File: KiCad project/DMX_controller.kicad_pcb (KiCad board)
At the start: 2 copper layers, 8 parts, among them J1 DMX_output, SW1 SW_Push_DPDT, U1 TTL_to_RS485_transceiver

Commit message: Make a real PCB!
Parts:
- added REF**: MountingHole_3.2mm_M3, MountingHole:MountingHole_3.2mm_M3, F.Cu at (53.3, 43.2)
- added REF**: MountingHole_3.2mm_M3, MountingHole:MountingHole_3.2mm_M3, F.Cu at (172.7, 149.9)
- added REF**: MountingHole_3.2mm_M3, MountingHole:MountingHole_3.2mm_M3, F.Cu at (53.3, 149.9)
- added REF**: MountingHole_3.2mm_M3, MountingHole:MountingHole_3.2mm_M3, F.Cu at (172.7, 43.2)
- RV3: value slider_3_hue -> slider_3_saturation
- RV4: value slider_4_saturation -> slider_4_hue
- moved U1 31.4 mm to (149.9, 98.9), turned to -90 degrees
- moved J1 20.5 mm to (155.1, 53.3)
- moved SW1 14.4 mm to (154.6, 103.1), turned to 90 degrees
- moved A1 9.16 mm to (149.9, 91.4)
- moved RV3 2.54 mm to (96.2, 52.3)
- moved RV4 2.54 mm to (114.5, 52.3)
- moved RV2 2.54 mm to (78.7, 52.3)
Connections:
- net /5V renamed +5V
- A1 pad 29: /GND -> unconnected-(A1-Pad29)
- A1 pad 4: /GND -> GND
- RV1 pad 1: /GND -> GND
- RV2 pad 1: /GND -> GND
- RV3 pad 1: /GND -> GND
- RV4 pad 1: /GND -> GND
- U1 pad 4: /GND -> GND
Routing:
- net GND: track 0.00 -> 132.6 mm
- net +5V: track 0.00 -> 126.3 mm
- net Net-(J1-Pad3): track 0.00 -> 121.1 mm
- net Net-(J1-Pad2): track 0.00 -> 107.4 mm
- net /A0: track 0.00 -> 97.3 mm
- net Net-(J1-Pad1): track 0.00 -> 90.6 mm
- net /A1: track 0.00 -> 87.6 mm
- net /A2: track 0.00 -> 77.8 mm
- net /A3: track 0.00 -> 67.7 mm
- net Net-(SW1-Pad4): track 0.00 -> 19.5 mm
- net Net-(SW1-Pad1): track 0.00 -> 14.0 mm
- net /RX: track 0.00 -> 13.8 mm
- net /TX: track 0.00 -> 9.57 mm
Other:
- board outline added: 134.6 x 121.9 mm
- board text added: "CCT"
- board text added: "DMX +"
- board text added: "DMX -"
- board text added: "DMX GND"
- board text added: "DMX controller"
- board text added: "DMX<---->Programming"
- board text added: "Dim"
- board text added: "Hue"
- board text added: "Revision 1"
- board text added: "Satur"
- board text added: "USB here"
- board text added: "ation"

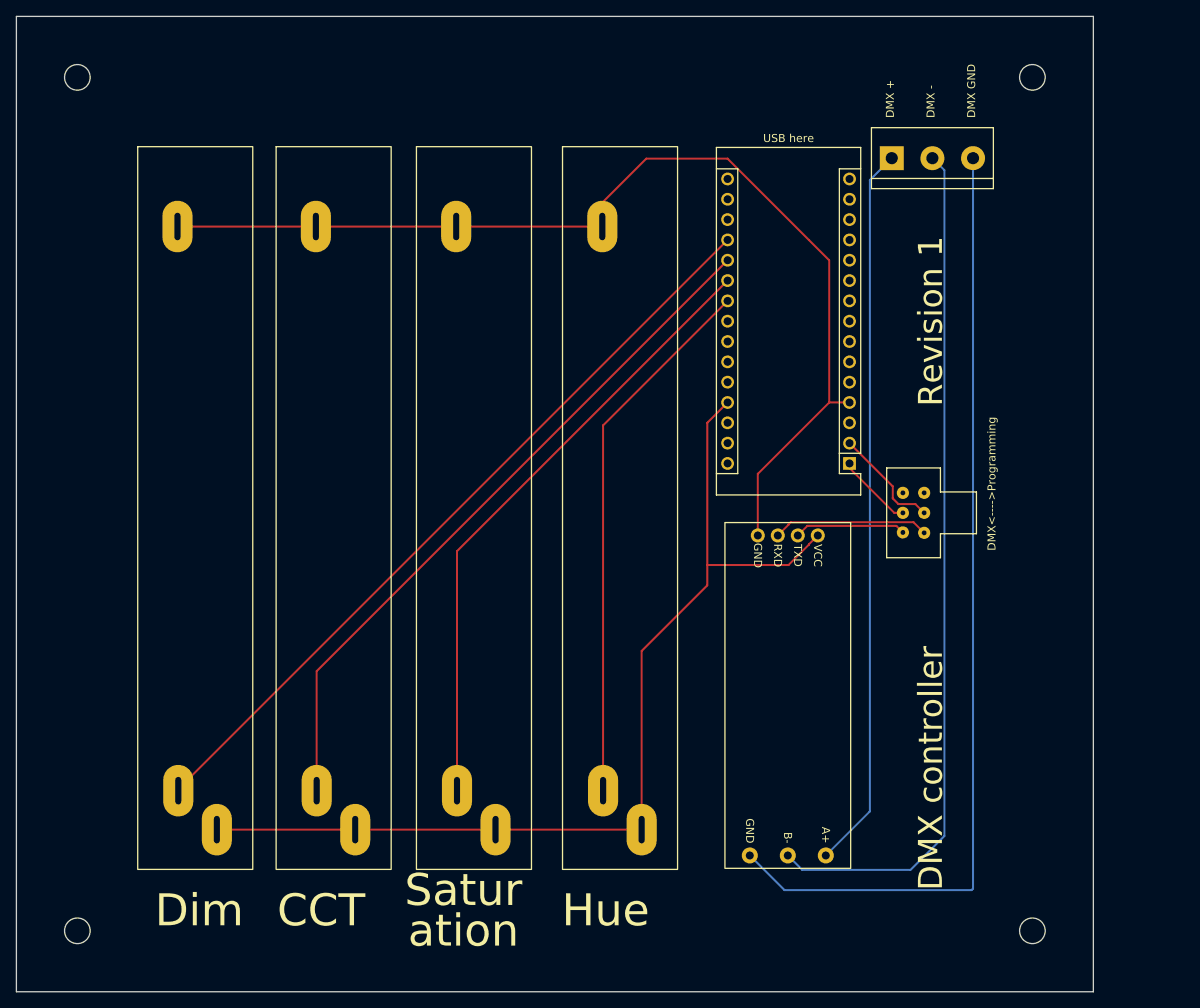
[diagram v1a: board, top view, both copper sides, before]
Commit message: Correct slide potentiometer pin numbering
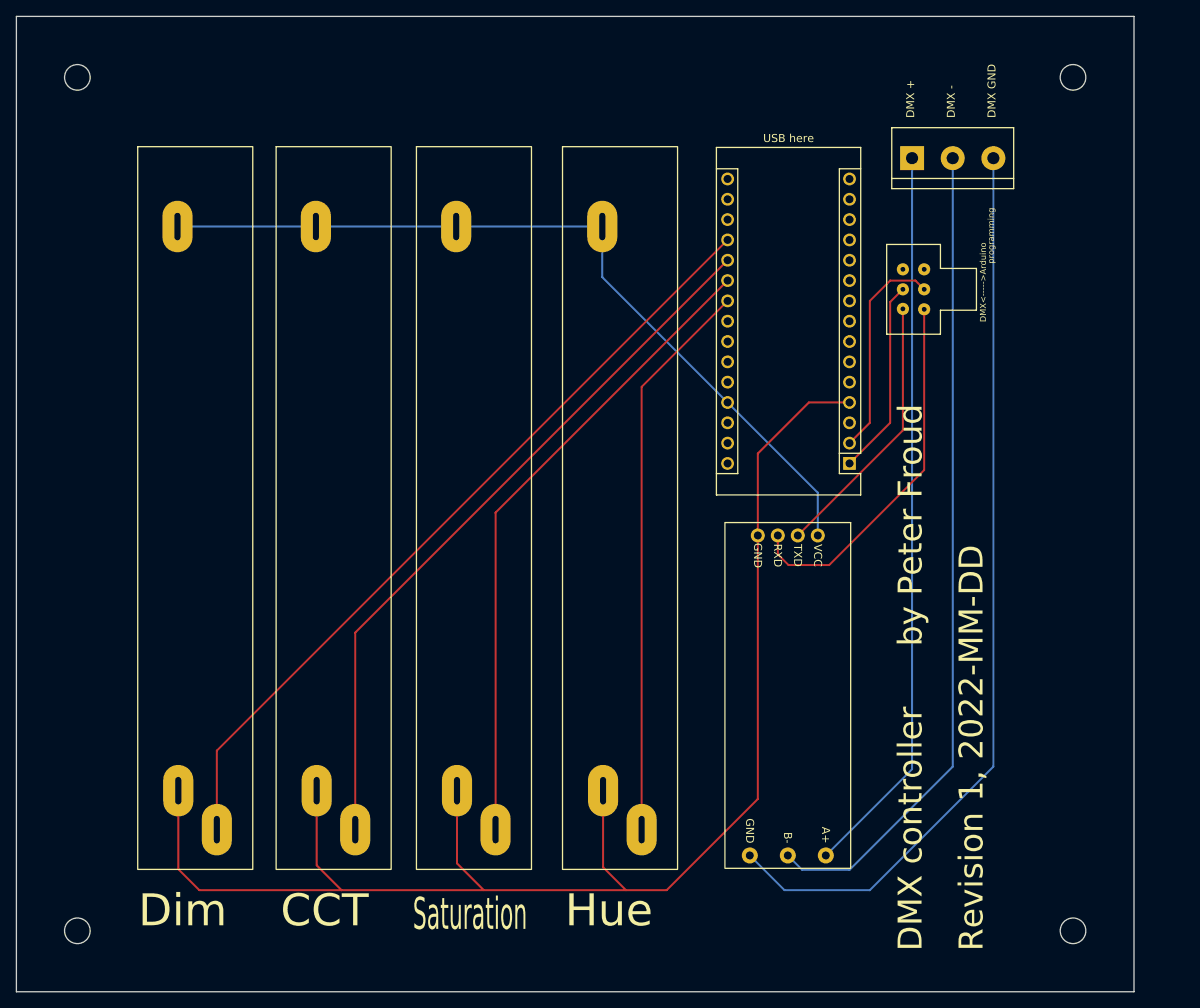
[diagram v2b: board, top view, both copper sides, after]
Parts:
- moved SW1 27.9 mm to (154.6, 75.2)
- moved MH2 5.08 mm to (177.8, 43.2)
- moved MH3 5.08 mm to (177.8, 149.9)
- moved J1 2.54 mm to (157.7, 53.3)
- renumbered REF** to MH1, REF** to MH2, REF** to MH3, REF** to MH4
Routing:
- net GND: track 132.6 -> 186.5 mm
- net Net-(SW1-Pad4): track 19.5 -> 46.2 mm
- net +5V: track 126.3 -> 102.9 mm
- net Net-(SW1-Pad1): track 14.0 -> 33.8 mm
- net /TX: track 9.57 -> 24.5 mm
- net /RX: track 13.8 -> 27.1 mm
- net Net-(J1-Pad3): track 121.1 -> 114.7 mm
- net Net-(J1-Pad2): track 107.4 -> 102.8 mm
- net /A3: track 67.7 -> 70.5 mm
- net /A2: track 77.8 -> 80.6 mm
- net /A0: track 97.3 -> 100.2 mm
- net /A1: track 87.6 -> 90.5 mm
- net Net-(J1-Pad1): track 90.6 -> 91.6 mm
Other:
- board size 134.6 x 121.9 mm -> 139.7 x 121.9 mm
- board text added: "DMX<----->Arduino"
- board text added: "Revision 1, 2022-MM-DD"
- board text added: "Saturation"
- board text added: "by Peter Froud"
- board text added: "programming"
- board text removed: "DMX<---->Programming"
- board text removed: "Revision 1"
- board text removed: "Satur"
- board text removed: "ation"

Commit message: Increase track width from 0.25mm to 0.5mm
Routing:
- net /RX: track 27.1 -> 42.5 mm
- net Net-(J1-Pad3): track 114.7 -> 118.7 mm
- net Net-(J1-Pad2): track 102.8 -> 106.8 mm
- net Net-(J1-Pad1): track 91.6 -> 95.7 mm

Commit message: Set date stamp for revision 1
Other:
- board text added: "Revision 1, 2022-06-30"
- board text removed: "Revision 1, 2022-MM-DD"
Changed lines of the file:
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@@
     (effects (font (size 1 1) (thickness 0.15)) (justify left))
   )
-  (gr_text "Revision 1, 2022-MM-DD" (at 165.1 152.4 90) (layer "F.SilkS")
+  (gr_text "Revision 1, 2022-06-30" (at 165.1 152.4 90) (layer "F.SilkS")
     (effects (font (size 3 3) (thickness 0.3)) (justify left))
   )
@@
   (segment (start 134.62 83.82) (end 145.895255 95.095255) (width 0.5) (layer "B.Cu") (net 27))
   (segment (start 101.655 61.825) (end 84.115 61.825) (width 0.5) (layer "B.Cu") (net 27))
-  (segment (start 157.68 56.08) (end 157.68 53.28) (width 0.5) (layer "B.Cu") (net 30))
+  (segment (start 162.56 58.16) (end 157.68 53.28) (width 0.5) (layer "B.Cu") (net 30))
+  (segment (start 162.56 124.777204) (end 162.56 58.16) (width 0.5) (layer "B.Cu") (net 30))
   (segment (start 146.895255 140.441949) (end 162.56 124.777204) (width 0.5) (layer "B.Cu") (net 30))
-  (segment (start 162.56 124.777204) (end 162.56 60.96) (width 0.5) (layer "B.Cu") (net 30))
-  (segment (start 162.56 60.96) (end 157.68 56.08) (width 0.5) (layer "B.Cu") (net 30))
   (segment (start 167.64 58.16) (end 167.64 124.46) (width 0.5) (layer "B.Cu") (net 31))
   (segment (start 143.943306 142.24) (end 142.145255 140.441949) (width 0.5) (layer "B.Cu") (net 31))

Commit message: Add pads and vias to mounting holes
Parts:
- MH1, MH2, MH3, MH4: value MountingHole_3.2mm_M3 -> MountingHole_3.2mm_M3_Pad_Via; footprint MountingHole:MountingHole_3.2mm_M3 -> MountingHole:MountingHole_3.2mm_M3_Pad_Via
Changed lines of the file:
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@@
       (net 27 "+5V") (pinfunction "3") (pintype "passive"))
   )
-  (footprint "MountingHole:MountingHole_3.2mm_M3" (layer "F.Cu")
+  (footprint "MountingHole:MountingHole_3.2mm_M3_Pad_Via" (layer "F.Cu")
     (at 53.34 43.18)
-    (descr "Mounting Hole 3.2mm, no annular, M3")
-    (tags "mounting hole 3.2mm no annular m3")
-    (attr board_only exclude_from_pos_files exclude_from_bom)
+    (descr "Mounting Hole 3.2mm, M3")
+    (tags "mounting hole 3.2mm m3")
+    (attr board_only)
     (fp_text reference "MH1" (at 0 -4.2) (layer "F.SilkS") hide
       (effects (font (size 1 1) (thickness 0.15)))
     )
-    (fp_text value "MountingHole_3.2mm_M3" (at 0 4.2) (layer "F.Fab")
+    (fp_text value "MountingHole_3.2mm_M3_Pad_Via" (at 0 4.2) (layer "F.Fab")
       (effects (font (size 1 1) (thickness 0.15)))
     )
@@
     (fp_circle (center 0 0) (end 3.2 0) (layer "Cmts.User") (width 0.15) (fill none))
     (fp_circle (center 0 0) (end 3.45 0) (layer "F.CrtYd") (width 0.05) (fill none))
-    (pad "" np_thru_hole circle (at 0 0) (size 3.2 3.2) (drill 3.2) (layers *.Cu *.Mask))
+    (pad "1" thru_hole circle (at -2.4 0) (size 0.8 0.8) (drill 0.5) (layers *.Cu *.Mask))
+    (pad "1" thru_hole circle (at -1.697056 1.697056) (size 0.8 0.8) (drill 0.5) (layers *.Cu *.Mask))
+    (pad "1" thru_hole circle (at 2.4 0) (size 0.8 0.8) (drill 0.5) (layers *.Cu *.Mask))
+    (pad "1" thru_hole circle (at 0 2.4) (size 0.8 0.8) (drill 0.5) (layers *.Cu *.Mask))
+    (pad "1" thru_hole circle (at 0 -2.4) (size 0.8 0.8) (drill 0.5) (layers *.Cu *.Mask))
+    (pad "1" thru_hole circle (at -1.697056 -1.697056) (size 0.8 0.8) (drill 0.5) (layers *.Cu *.Mask))
+    (pad "1" thru_hole circle (at 0 0) (size 6.4 6.4) (drill 3.2) (layers *.Cu *.Mask))
+    (pad "1" thru_hole circle (at 1.697056 -1.697056) (size 0.8 0.8) (drill 0.5) (layers *.Cu *.Mask))
+    (pad "1" thru_hole circle (at 1.697056 1.697056) (size 0.8 0.8) (drill 0.5) (layers *.Cu *.Mask))
   )
   (footprint "Module:Arduino_Nano" (layer "F.Cu")
@@
       (net 32 "Net-(J1-Pad3)") (pinfunction "GND") (pintype "power_in"))
   )
-  (footprint "MountingHole:MountingHole_3.2mm_M3" (layer "F.Cu")
+  (footprint "MountingHole:MountingHole_3.2mm_M3_Pad_Via" (layer "F.Cu")
     (at 177.8 149.86)
-    (descr "Mounting Hole 3.2mm, no annular, M3")
-    (tags "mounting hole 3.2mm no annular m3")
-    (attr board_only exclude_from_pos_files exclude_from_bom)
+    (descr "Mounting Hole 3.2mm, M3")
+    (tags "mounting hole 3.2mm m3")
+    (attr board_only)
     (fp_text reference "MH3" (at 0 -4.2) (layer "F.SilkS") hide
       (effects (font (size 1 1) (thickness 0.15)))
     )
-    (fp_text value "MountingHole_3.2mm_M3" (at 0 4.2) (layer "F.Fab")
+    (fp_text value "MountingHole_3.2mm_M3_Pad_Via" (at 0 4.2) (layer "F.Fab")
       (effects (font (size 1 1) (thickness 0.15)))
     )
@@
     (fp_circle (center 0 0) (end 3.2 0) (layer "Cmts.User") (width 0.15) (fill none))
     (fp_circle (center 0 0) (end 3.45 0) (layer "F.CrtYd") (width 0.05) (fill none))
-    (pad "" np_thru_hole circle (at 0 0) (size 3.2 3.2) (drill 3.2) (layers *.Cu *.Mask))
-  )
-  (footprint "MountingHole:MountingHole_3.2mm_M3" (layer "F.Cu")
+    (pad "1" thru_hole circle (at 1.697056 1.697056) (size 0.8 0.8) (drill 0.5) (layers *.Cu *.Mask))
+    (pad "1" thru_hole circle (at 0 -2.4) (size 0.8 0.8) (drill 0.5) (layers *.Cu *.Mask))
+    (pad "1" thru_hole circle (at 0 0) (size 6.4 6.4) (drill 3.2) (layers *.Cu *.Mask))
+    (pad "1" thru_hole circle (at 0 2.4) (size 0.8 0.8) (drill 0.5) (layers *.Cu *.Mask))
+    (pad "1" thru_hole circle (at 1.697056 -1.697056) (size 0.8 0.8) (drill 0.5) (layers *.Cu *.Mask))
+    (pad "1" thru_hole circle (at -1.697056 -1.697056) (size 0.8 0.8) (drill 0.5) (layers *.Cu *.Mask))
+    (pad "1" thru_hole circle (at 2.4 0) (size 0.8 0.8) (drill 0.5) (layers *.Cu *.Mask))
+    (pad "1" thru_hole circle (at -1.697056 1.697056) (size 0.8 0.8) (drill 0.5) (layers *.Cu *.Mask))
+    (pad "1" thru_hole circle (at -2.4 0) (size 0.8 0.8) (drill 0.5) (layers *.Cu *.Mask))
+  )
+  (footprint "MountingHole:MountingHole_3.2mm_M3_Pad_Via" (layer "F.Cu")
     (at 53.34 149.86)
-    (descr "Mounting Hole 3.2mm, no annular, M3")
-    (tags "mounting hole 3.2mm no annular m3")
-    (attr board_only exclude_from_pos_files exclude_from_bom)
+    (descr "Mounting Hole 3.2mm, M3")
+    (tags "mounting hole 3.2mm m3")
+    (attr board_only)
     (fp_text reference "MH4" (at 0 -4.2) (layer "F.SilkS") hide
       (effects (font (size 1 1) (thickness 0.15)))
     )
-    (fp_text value "MountingHole_3.2mm_M3" (at 0 4.2) (layer "F.Fab")
+    (fp_text value "MountingHole_3.2mm_M3_Pad_Via" (at 0 4.2) (layer "F.Fab")
       (effects (font (size 1 1) (thickness 0.15)))
     )
@@
     (fp_circle (center 0 0) (end 3.2 0) (layer "Cmts.User") (width 0.15) (fill none))
     (fp_circle (center 0 0) (end 3.45 0) (layer "F.CrtYd") (width 0.05) (fill none))
-    (pad "" np_thru_hole circle (at 0 0) (size 3.2 3.2) (drill 3.2) (layers *.Cu *.Mask))
-  )
-  (footprint "MountingHole:MountingHole_3.2mm_M3" (layer "F.Cu")
+    (pad "1" thru_hole circle (at 0 2.4) (size 0.8 0.8) (drill 0.5) (layers *.Cu *.Mask))
+    (pad "1" thru_hole circle (at -1.697056 -1.697056) (size 0.8 0.8) (drill 0.5) (layers *.Cu *.Mask))
+    (pad "1" thru_hole circle (at 0 0) (size 6.4 6.4) (drill 3.2) (layers *.Cu *.Mask))
+    (pad "1" thru_hole circle (at 1.697056 1.697056) (size 0.8 0.8) (drill 0.5) (layers *.Cu *.Mask))
+    (pad "1" thru_hole circle (at 1.697056 -1.697056) (size 0.8 0.8) (drill 0.5) (layers *.Cu *.Mask))
+    (pad "1" thru_hole circle (at -2.4 0) (size 0.8 0.8) (drill 0.5) (layers *.Cu *.Mask))
+    (pad "1" thru_hole circle (at 2.4 0) (size 0.8 0.8) (drill 0.5) (layers *.Cu *.Mask))
+    (pad "1" thru_hole circle (at 0 -2.4) (size 0.8 0.8) (drill 0.5) (layers *.Cu *.Mask))
+    (pad "1" thru_hole circle (at -1.697056 1.697056) (size 0.8 0.8) (drill 0.5) (layers *.Cu *.Mask))
+  )
+  (footprint "MountingHole:MountingHole_3.2mm_M3_Pad_Via" (layer "F.Cu")
     (at 177.8 43.18)
-    (descr "Mounting Hole 3.2mm, no annular, M3")
-    (tags "mounting hole 3.2mm no annular m3")
-    (attr board_only exclude_from_pos_files exclude_from_bom)
+    (descr "Mounting Hole 3.2mm, M3")
+    (tags "mounting hole 3.2mm m3")
+    (attr board_only)
     (fp_text reference "MH2" (at 0 -4.2) (layer "F.SilkS") hide
       (effects (font (size 1 1) (thickness 0.15)))
     )
-    (fp_text value "MountingHole_3.2mm_M3" (at 0 4.2) (layer "F.Fab")
+    (fp_text value "MountingHole_3.2mm_M3_Pad_Via" (at 0 4.2) (layer "F.Fab")
       (effects (font (size 1 1) (thickness 0.15)))
     )
@@
     (fp_circle (center 0 0) (end 3.2 0) (layer "Cmts.User") (width 0.15) (fill none))
     (fp_circle (center 0 0) (end 3.45 0) (layer "F.CrtYd") (width 0.05) (fill none))
-    (pad "" np_thru_hole circle (at 0 0) (size 3.2 3.2) (drill 3.2) (layers *.Cu *.Mask))
+    (pad "1" thru_hole circle (at 0 0) (size 6.4 6.4) (drill 3.2) (layers *.Cu *.Mask))
+    (pad "1" thru_hole circle (at 2.4 0) (size 0.8 0.8) (drill 0.5) (layers *.Cu *.Mask))
+    (pad "1" thru_hole circle (at 0 2.4) (size 0.8 0.8) (drill 0.5) (layers *.Cu *.Mask))
+    (pad "1" thru_hole circle (at -2.4 0) (size 0.8 0.8) (drill 0.5) (layers *.Cu *.Mask))
+    (pad "1" thru_hole circle (at -1.697056 -1.697056) (size 0.8 0.8) (drill 0.5) (layers *.Cu *.Mask))
+    (pad "1" thru_hole circle (at 1.697056 -1.697056) (size 0.8 0.8) (drill 0.5) (layers *.Cu *.Mask))
+    (pad "1" thru_hole circle (at 0 -2.4) (size 0.8 0.8) (drill 0.5) (layers *.Cu *.Mask))
+    (pad "1" thru_hole circle (at -1.697056 1.697056) (size 0.8 0.8) (drill 0.5) (layers *.Cu *.Mask))
+    (pad "1" thru_hole circle (at 1.697056 1.697056) (size 0.8 0.8) (drill 0.5) (layers *.Cu *.Mask))
   )
   (footprint "TerminalBlock:TerminalBlock_bornier-3_P5.08mm" (layer "F.Cu")
